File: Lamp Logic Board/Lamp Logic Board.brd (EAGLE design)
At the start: 68.6 x 65.7 mm, 44 parts, among them U1 ESP32-WROVER-IB, U2 SN74HCT245DWR, U4 LM50, U6 MSGEQ7DIL

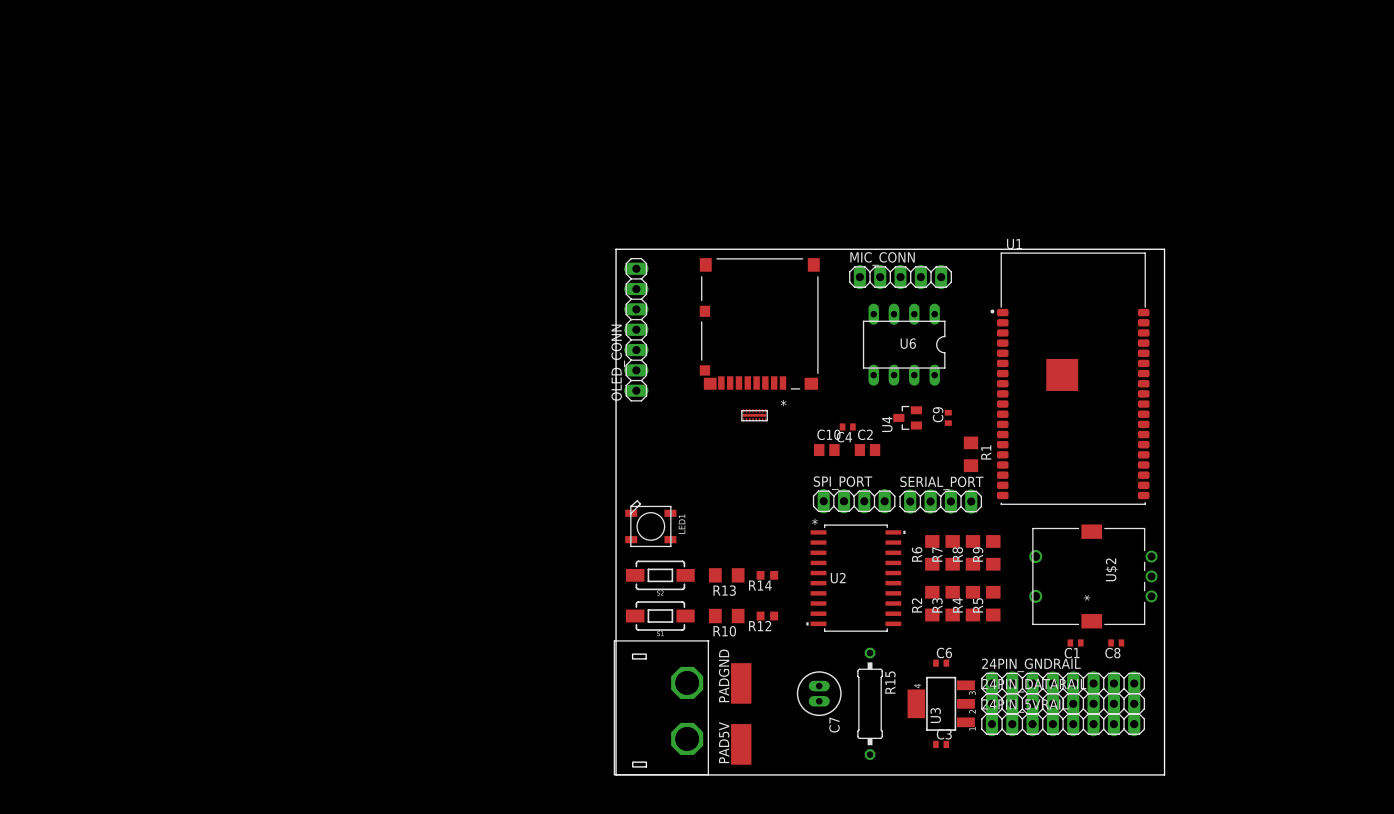
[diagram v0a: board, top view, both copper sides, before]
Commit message: Add files via upload
Uploading a version, that does not have a messed up board file.
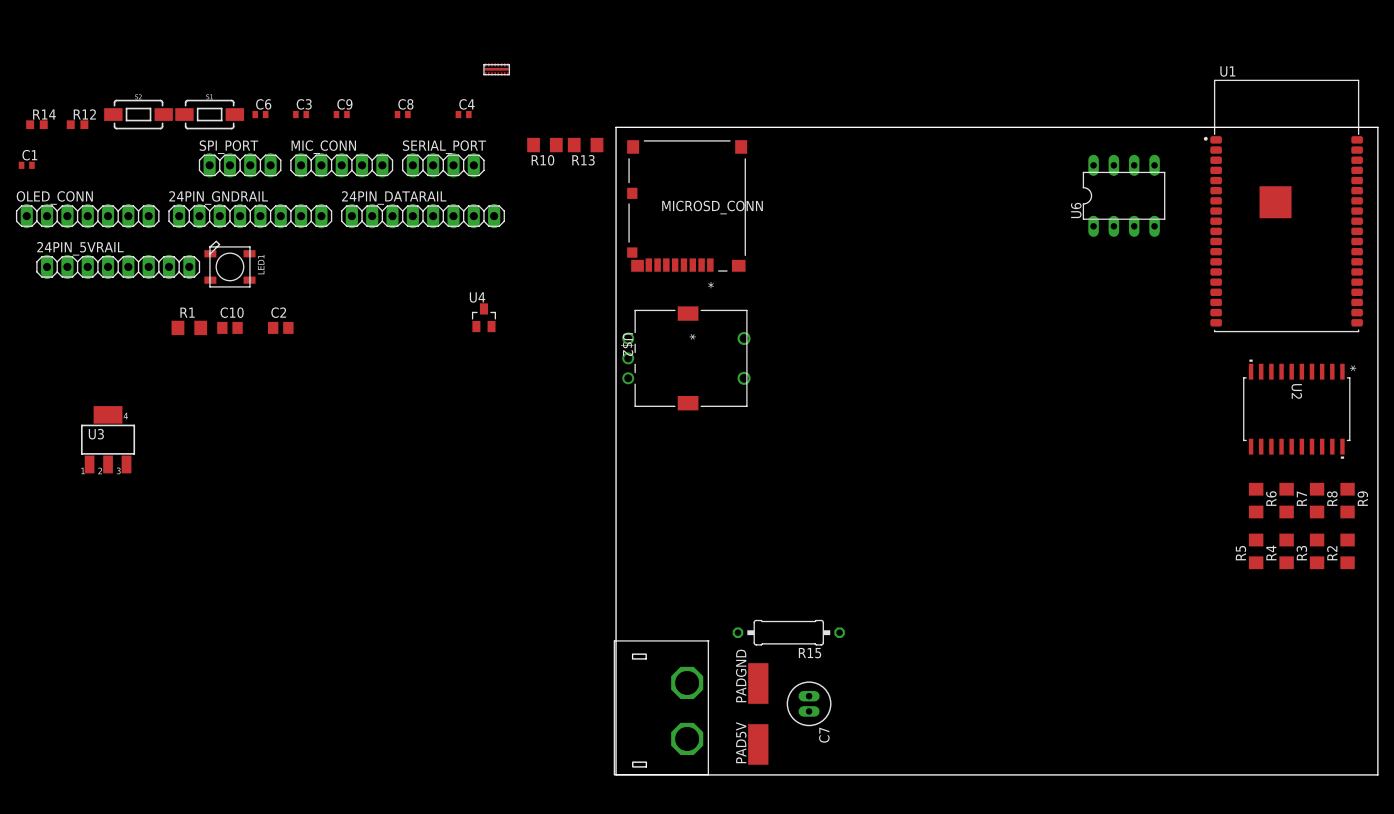
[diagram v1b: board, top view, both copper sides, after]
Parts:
- moved C1 144.1 mm to (-73.7, 76.2), turned to 0 degrees
- moved 24PIN_5VRAIL 131.2 mm to (-62.2, 63.5)
- moved 24PIN_GNDRAIL 117.2 mm to (-45.7, 69.8)
- moved C3 112.3 mm to (-39.4, 82.5)
- moved C8 111.0 mm to (-26.7, 82.5), turned to 0 degrees
- moved C6 109.3 mm to (-44.5, 82.5)
- moved U3 109.2 mm to (-63.5, 41.9), turned to 0 degrees
- moved R14 107.3 mm to (-72.4, 81.3), turned to 0 degrees
- moved R12 105.9 mm to (-67.3, 81.3), turned to 0 degrees
- moved 24PIN_DATARAIL 100.6 mm to (-24.1, 69.8)
- moved R1 99.0 mm to (-53.3, 55.9), turned to 0 degrees
- moved SPI_PORT 87.5 mm to (-47.0, 76.2)
- moved S2 87.0 mm to (-59.7, 82.5), turned to 0 degrees
- moved U$2 85.6 mm to (-6.35, 52.1), turned to 270 degrees
- moved C9 84.8 mm to (-34.3, 82.5), turned to 0 degrees
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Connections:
- removed net N$1: MICROSD_CONN.10
- new net N$5: U1.26
- net GAIN: no longer U1.6
- net GND: now also MICROSD_CONN.10
- net MIC: now also U1.5; no longer U1.7
- net MSGEQ_OUT: now also U1.6; no longer U1.26
- net MSGEQ_STROBE: now also U1.7
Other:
- board size 68.6 x 65.7 mm -> 95.2 x 81 mm

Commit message: It's the £2 one.
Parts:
- removed 24PIN_5VRAIL, 24PIN_DATARAIL, 24PIN_GNDRAIL: (no value), pinhead:1X08
- removed OLED_CONN: (no value), pinhead:1X07
- removed SERIAL_PORT, SPI_PORT: (no value), pinhead:1X04
- added PAD5V1, PADGND1: (no value), wirepad:SMD2,54-5,08
- added R11: (no value), resistor:R0603
- added R16: 330, resistor:R1206
- added U$4: 3X8PINHEAD, 3X8PINHEAD:3X8PINHEAD
- added U$5: 2X4PINHEAD, 2X4PINHEAD:2X4PINHEAD
- added U5: SPIOLED_STANDOFF, SPIOLED-STANDOFF:SPIOLED_STADOFF
- moved R14 103.0 mm to (17.3, 30.6), turned to 180 degrees
- moved R1 94.0 mm to (38.0, 78.2), turned to 270 degrees
- moved C1 93.8 mm to (10.6, 35.0), turned to 270 degrees
- moved S2 87.4 mm to (8.03, 27.2), turned to 180 degrees
- moved R12 82.4 mm to (12.6, 61.1), turned to 90 degrees
- moved U3 79.0 mm to (14.9, 51.8)
- moved R2 70.3 mm to (21.2, 24.6), turned to 270 degrees
- moved C6 68.0 mm to (13.0, 46.2), turned to 180 degrees
- moved C3 66.9 mm to (19.1, 50.0), turned to 90 degrees
- moved C10 65.0 mm to (11.2, 82.3)
- moved S1 64.7 mm to (9.25, 58.4), turned to 270 degrees
- moved R3 63.9 mm to (23.8, 24.6), turned to 270 degrees
- moved C9 61.4 mm to (20.3, 54.5)
- moved U1 58.9 mm to (25.2, 76.8)
- moved U$3 58.4 mm to (35.4, 60.9)
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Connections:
- removed net N$16: R3.1, U2.17
- removed net N$17: R4.1, U2.16
- removed net N$18: R5.1, U2.15
- removed net N$19: R6.1, U2.14
- removed net N$20: R7.1, U2.13
- removed net N$21: R8.1, U2.12
- removed net N$22: R9.1, U2.11
- new net N$1: R9.1, U2.18
- new net N$10: R7.1, U2.16
- new net N$11: R6.1, U2.15
- new net N$12: R5.1, U2.14
- new net N$13: R4.1, U2.13
- new net N$14: R3.1, U2.12
- new net N$6: R8.1, U2.17
- new net ROTARY_BUTTON_IN: R11.1, R16.2, U1.4
- net CS: now also U$5.CS; no longer SPI_PORT.2
- net GND: now also PADGND1.1, U$2.4, U$4.1, U$4.2, U$4.3, U$4.4, U$4.5, U$4.6, U$4.7, U$4.8, U$5.GND, U5.GND; no longer 24PIN_GNDRAIL.1, 24PIN_GNDRAIL.2, 24PIN_GNDRAIL.3, 24PIN_GNDRAIL.4, 24PIN_GNDRAIL.5, 24PIN_GNDRAIL.6, 24PIN_GNDRAIL.7, 24PIN_GNDRAIL.8, OLED_CONN.1, SERIAL_PORT.1
- net LEDS1_3V3: now also U1.23; no longer U1.14
- net LEDS1_5V: now also U$4.9; no longer 24PIN_DATARAIL.1
- net LEDS2_3V3: now also U1.30; no longer U1.16
- net LEDS2_5V: now also U$4.10; no longer 24PIN_DATARAIL.2
- net LEDS3_3V3: now also U1.31; no longer U1.13
- net LEDS3_5V: now also U$4.11; no longer 24PIN_DATARAIL.3
- net LEDS4_3V3: now also U1.33; no longer U1.23
- net LEDS4_5V: now also U$4.12; no longer 24PIN_DATARAIL.4
- net LEDS5_3V3: now also U1.36; no longer U1.30
- net LEDS5_5V: now also U$4.13; no longer 24PIN_DATARAIL.5
- net LEDS6_3V3: now also U1.13; no longer U1.31
- net LEDS6_5V: now also U$4.14; no longer 24PIN_DATARAIL.6
- net LEDS7_3V3: now also U1.14; no longer U1.33
- net LEDS7_5V: now also U$4.15; no longer 24PIN_DATARAIL.7
- net LEDS8_3V3: now also U1.16; no longer U1.36
- net LEDS8_5V: now also U$4.16; no longer 24PIN_DATARAIL.8
- net MISO: now also U$5.MISO; no longer SPI_PORT.4
- net MOSI: now also U$5.MOSI, U5.DIN; no longer OLED_CONN.4, SPI_PORT.3
- net N$15: now also U2.11; no longer U2.18
- net N$5: now also R16.1, U$2.5; no longer U1.26
- net OLED_CS: now also U5.CS; no longer OLED_CONN.7
- net OLED_DC: now also U5.DC; no longer OLED_CONN.6
- net OLED_RESET: now also U5.RST; no longer OLED_CONN.5
- net OUTA: now also U1.11; no longer U1.12
- net OUTB: now also U1.12; no longer U1.11
- net RX0: now also U$5.RX0; no longer SERIAL_PORT.3
- net SCK: now also U$5.SCK, U5.CLK; no longer OLED_CONN.3, SPI_PORT.1
- net TX0: now also U$5.TX0; no longer SERIAL_PORT.4
- net VDD3V3: now also R11.2, U$5.VDD, U5.VCC; no longer OLED_CONN.2, SERIAL_PORT.2
- net VDD3V3_TEMP_OUT: now also U1.26
- net VDD5V: now also PAD5V1.1, U$4.17, U$4.18, U$4.19, U$4.20, U$4.21, U$4.22, U$4.23, U$4.24; no longer 24PIN_5VRAIL.1, 24PIN_5VRAIL.2, 24PIN_5VRAIL.3, 24PIN_5VRAIL.4, 24PIN_5VRAIL.5, 24PIN_5VRAIL.6, 24PIN_5VRAIL.7, 24PIN_5VRAIL.8
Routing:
- net VDD5V: track 0.00 -> 265.2 mm
- net VDD3V3: track 0.00 -> 172.1 mm
- net GND: track 0.00 -> 89.3 mm
- net IO0: track 0.00 -> 70.7 mm, vias 0 -> 2
- net ROTARY_BUTTON_IN: track 0.00 -> 59.9 mm, vias 0 -> 2
- net TX0: track 0.00 -> 58.0 mm, vias 0 -> 2
- net RX0: track 0.00 -> 52.9 mm, vias 0 -> 4
- net LEDS5_3V3: track 0.00 -> 52.0 mm, vias 0 -> 2
- net LEDSDIAG_3V3: track 0.00 -> 51.0 mm, vias 0 -> 2
- net SCK: track 0.00 -> 49.4 mm, vias 0 -> 3
- net LEDS4_3V3: track 0.00 -> 47.8 mm, vias 0 -> 2
- net LEDS3_3V3: track 0.00 -> 45.7 mm, vias 0 -> 2
- net OUTA: track 0.00 -> 44.8 mm, vias 0 -> 1
- net LEDS2_3V3: track 0.00 -> 44.7 mm, vias 0 -> 2
- net LEDS6_3V3: track 0.00 -> 44.4 mm, vias 0 -> 2
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- added copper zone on layer 1, net GND
- added copper zone on layer 16, net GND
- added copper zone on layer 16, net VDD5V
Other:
- board size 95.2 x 81 mm -> 41.3 x 85.5 mm
